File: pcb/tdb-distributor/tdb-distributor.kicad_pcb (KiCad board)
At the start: 2 copper layers, 81.3 x 63.5 mm, 15 parts, among them J1 Conn_02x07_Odd_Even, J2 Conn_02x07_Odd_Even, J3 Conn_02x07_Odd_Even, J4 Conn_02x07_Odd_Even, J5 Screw_Terminal_01x03, J6 Conn_01x06_Pin, J7 Conn_01x07_Pin, J8 Conn_01x08_Pin, U1 LM317_TO-220

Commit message: Add labels to power input
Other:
- board text added: "15V"
- board text added: "5V"
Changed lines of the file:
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@@
+    (effects (font (size 1 1) (thickness 0.15)) (justify left bottom))
+  )
+  (gr_text "15V" (at 138.43 41.91 -90) (layer "F.SilkS")
+    (effects (font (size 1 1) (thickness 0.15)) (justify left bottom))
+  )
+  (gr_text "5V" (at 138.43 36.83 -90) (layer "F.SilkS")
     (effects (font (size 1 1) (thickness 0.15)) (justify left bottom))
   )
@@
     (effects (font (size 1 1) (thickness 0.15)) (justify left bottom))
   )
+  (gr_text "GND\n" (at 138.43 46.99 -90) (layer "F.SilkS")
+    (effects (font (size 1 1) (thickness 0.15)) (justify left bottom))
+  )

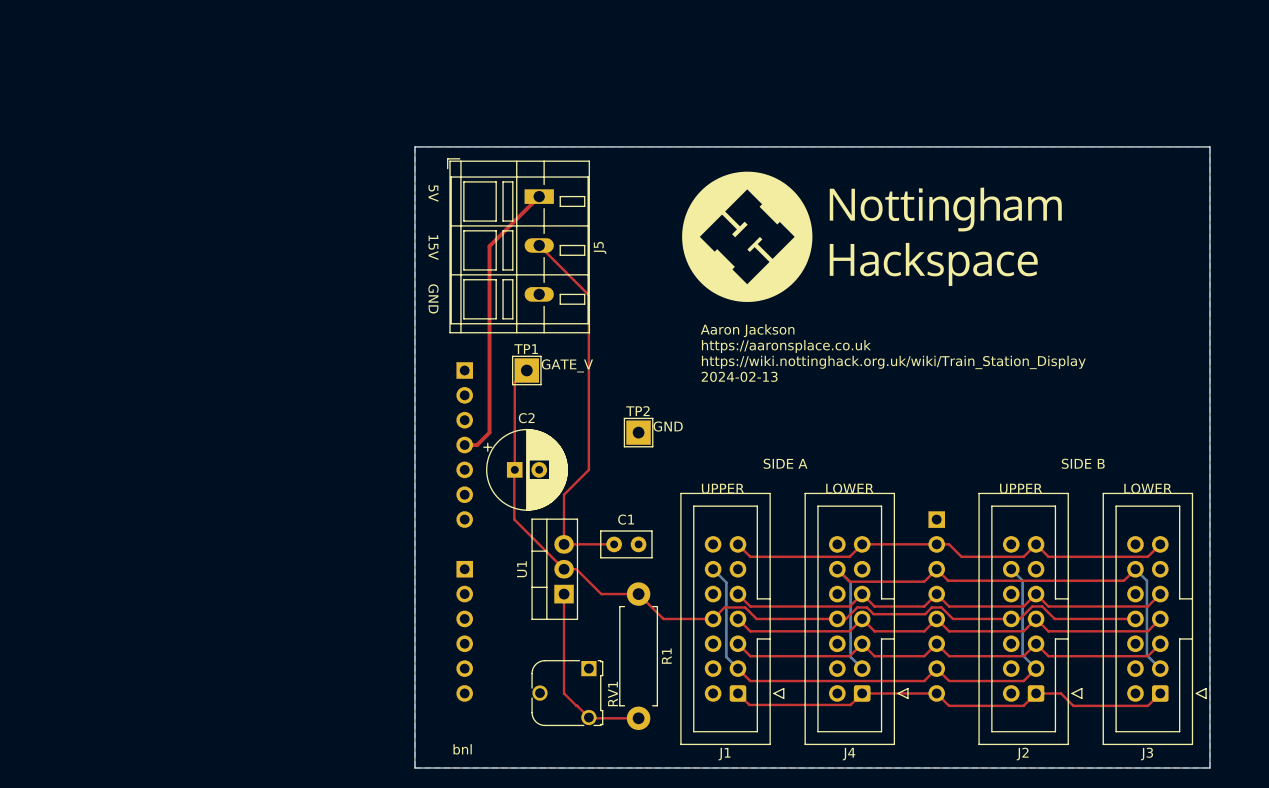
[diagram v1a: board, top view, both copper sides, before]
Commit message: Board redesign
Includes R7 MPU and WizNet
Adds buffer chips to hopefully support both sides of the display
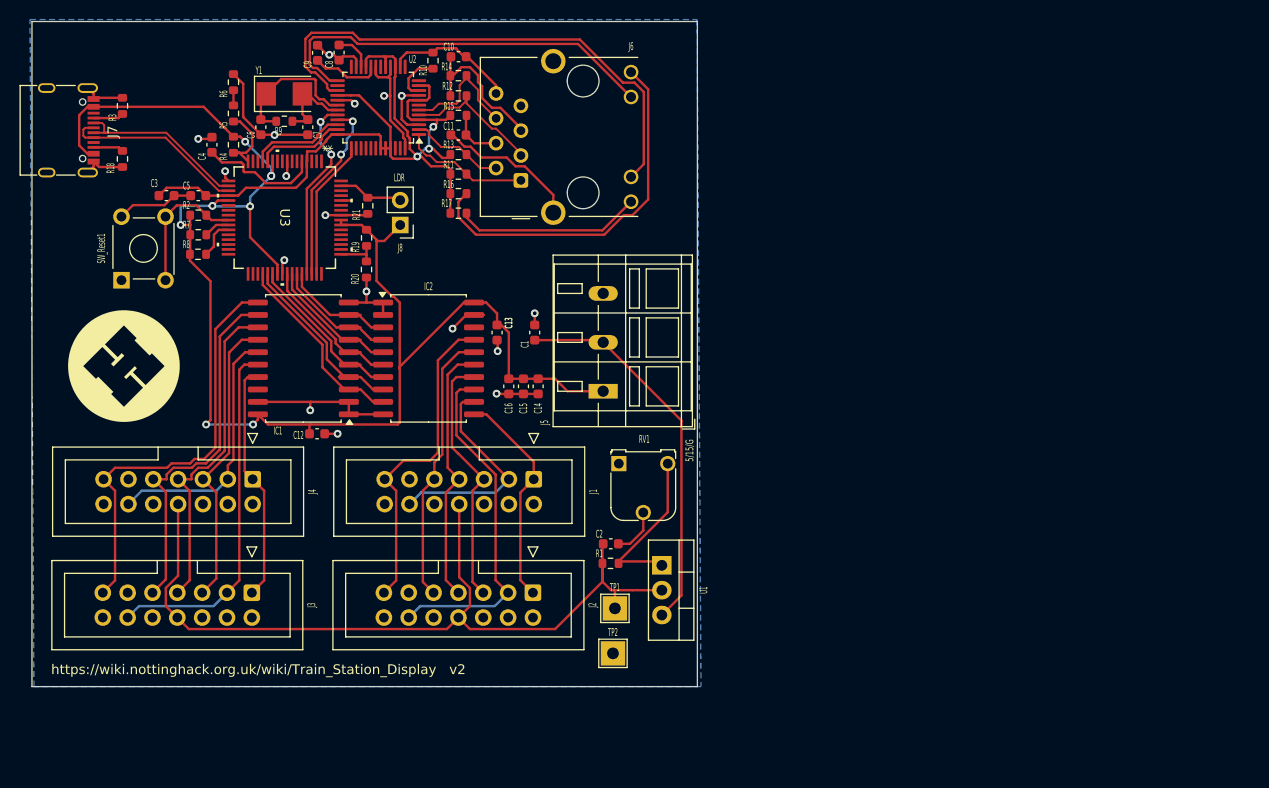
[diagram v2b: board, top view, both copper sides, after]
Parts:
- added C10: 10n, Capacitor_SMD:C_0603_1608Metric, F.Cu at (141.6, 23.8)
- added C11: 22n, Capacitor_SMD:C_0603_1608Metric, F.Cu at (141.6, 31.8)
- added C12: 4.7u, Capacitor_SMD:C_0603_1608Metric, F.Cu at (127.2, 62.4)
- added C13: 4.7u, Capacitor_SMD:C_0603_1608Metric, F.Cu at (145.6, 52.0)
- added C14: 22u, Capacitor_SMD:C_0603_1608Metric, F.Cu at (149.8, 57.5)
- added C15: 22u, Capacitor_SMD:C_0603_1608Metric, F.Cu at (148.2, 57.5)
- added C16: 22u, Capacitor_SMD:C_0603_1608Metric, F.Cu at (146.8, 57.5)
- added C3: 4.7u, Capacitor_SMD:C_0603_1608Metric, F.Cu at (111.8, 38.0)
- added C4: 4.7u, Capacitor_SMD:C_0603_1608Metric, F.Cu at (116.4, 32.8)
- added C5: 4.7u, Capacitor_SMD:C_0603_1608Metric, F.Cu at (115.0, 38.0)
- added C6: 18p, Capacitor_SMD:C_0603_1608Metric, F.Cu at (121.4, 31.0)
- added C7: 18p, Capacitor_SMD:C_0603_1608Metric, F.Cu at (126.2, 31.0)
- added C8: 10n, Capacitor_SMD:C_0603_1608Metric, F.Cu at (129.4, 23.4)
- added C9: 4.7u, Capacitor_SMD:C_0603_1608Metric, F.Cu at (127.2, 23.4)
- added IC1: 74HC541D,653, Package_SO:SOIC-20W_7.5x12.8mm_P1.27mm, F.Cu at (125.7, 54.6)
- added IC2: 74HC541D,653, Package_SO:SOIC-20W_7.5x12.8mm_P1.27mm, F.Cu at (138.5, 54.6)
- added R10: 12.4k, Resistor_SMD:R_0603_1608Metric, F.Cu at (139.0, 24.2)
- added R11: 49.9, Resistor_SMD:R_0603_1608Metric, F.Cu at (141.6, 35.8)
- added R12: 49.9, Resistor_SMD:R_0603_1608Metric, F.Cu at (141.6, 27.8)
- added R13: 49.9, Resistor_SMD:R_0603_1608Metric, F.Cu at (141.6, 33.8)
- added R14: 49.9, Resistor_SMD:R_0603_1608Metric, F.Cu at (141.6, 25.7)
- added R15: 10, Resistor_SMD:R_0603_1608Metric, F.Cu at (141.6, 29.8)
- added R16: 100, Resistor_SMD:R_0603_1608Metric, F.Cu at (141.6, 37.8)
- added R17: 100, Resistor_SMD:R_0603_1608Metric, F.Cu at (141.6, 39.8)
- added R18: 5.1k, Resistor_SMD:R_0603_1608Metric, F.Cu at (107.2, 34.2)
- added R19: 100k, Resistor_SMD:R_0603_1608Metric, F.Cu at (132.2, 42.3)
- added R2: 5.1k, Resistor_SMD:R_0603_1608Metric, F.Cu at (115.0, 40.0)
- added R20: 5.1k, Resistor_SMD:R_0603_1608Metric, F.Cu at (132.2, 45.5)
- added R21: 5.1k, Resistor_SMD:R_0603_1608Metric, F.Cu at (132.3, 39.0)
- added R3: 5.1k, Resistor_SMD:R_0603_1608Metric, F.Cu at (107.2, 28.8)
- added R4: 5.1k, Resistor_SMD:R_0603_1608Metric, F.Cu at (118.6, 32.8)
- added R5: 5.1k, Resistor_SMD:R_0603_1608Metric, F.Cu at (118.6, 29.6)
- added R6: 5.1k, Resistor_SMD:R_0603_1608Metric, F.Cu at (118.6, 26.4)
- added R7: 5.1k, Resistor_SMD:R_0603_1608Metric, F.Cu at (115.0, 42.0)
- added R8: 5.1k, Resistor_SMD:R_0603_1608Metric, F.Cu at (115.0, 44.0)
- added R9: 1M, Resistor_SMD:R_0603_1608Metric, F.Cu at (123.8, 30.4)
- added SW_Reset1: SW_Push, Button_Switch_THT:SW_TH_Tactile_Omron_B3F-10xx, F.Cu at (107.2, 46.6)
- added U2: W5500, Package_QFP:LQFP-48_7x7mm_P0.5mm, F.Cu at (133.4, 29.0)
- added U3: R7FA4M1AB3CFM, R7FA4M1AB3CFM:PLQP0064KB-C_REN, F.Cu at (123.8, 40.3)
- added Y1: 25M, Crystal:Crystal_SMD_5032-2Pin_5.0x3.2mm, F.Cu at (123.8, 27.6)
- C1: footprint Capacitor_THT:C_Disc_D5.0mm_W2.5mm_P2.50mm -> Capacitor_SMD:C_0603_1608Metric
- C2: footprint Capacitor_THT:CP_Radial_D8.0mm_P2.50mm -> Capacitor_SMD:C_0603_1608Metric
- J6: value Conn_01x06_Pin -> RJ45_Hanrun_HR911105A_Horizontal; footprint Connector_PinHeader_2.54mm:PinHeader_1x06_P2.54mm_Vertical -> Connector_RJ:RJ45_Hanrun_HR911105A_Horizontal; moved to F.Cu
- J7: value Conn_01x07_Pin -> USB_C_Receptacle_USB2.0_16P; footprint Connector_PinHeader_2.54mm:PinHeader_1x07_P2.54mm_Vertical -> Connector_USB:USB_C_Receptacle_G-Switch_GT-USB-7010ASV; moved to F.Cu
- J8: value Conn_01x08_Pin -> Conn_01x02; footprint Connector_PinHeader_2.54mm:PinHeader_1x08_P2.54mm_Vertical -> Connector_PinHeader_2.54mm:PinHeader_1x02_P2.54mm_Vertical; moved to F.Cu
- R1: footprint Resistor_THT:R_Axial_DIN0411_L9.9mm_D3.6mm_P12.70mm_Horizontal -> Resistor_SMD:R_0603_1608Metric
- moved J3 93.4 mm to (120.5, 78.6), turned to -90 degrees
- moved J4 66.1 mm to (120.6, 67.0), turned to -90 degrees
- moved J8 62.6 mm to (135.7, 41.0)
- moved J2 52.5 mm to (149.2, 78.6), turned to -90 degrees
- moved J7 48.4 mm to (100.6, 31.3), turned to -90 degrees
- moved J6 40.2 mm to (148.0, 36.4), turned to 90 degrees
- moved J1 30.3 mm to (149.3, 67.0), turned to -90 degrees
- moved TP1 25.9 mm to (157.6, 80.2)
- moved C1 23.1 mm to (149.4, 52.0), turned to 90 degrees
- moved TP2 22.7 mm to (157.4, 84.8)
- moved RV1 21.2 mm to (158.0, 65.4), turned to 0 degrees
- moved J5 20.9 mm to (156.4, 58.0), turned to 90 degrees
- moved C2 12.4 mm to (157.2, 73.6)
- moved U1 10.4 mm to (162.4, 75.8), turned to -90 degrees
- moved R1 4.25 mm to (157.2, 75.6), turned to 0 degrees
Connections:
- J1 pad 1: /CLOCK -> /bCLOCK
- J1 pad 11: GND -> unconnected-(J1-Pin_11-Pad11)
- J1 pad 12: /DATA_A -> /bDATA_A
- J1 pad 13: /STROBE -> /bSTROBE
- J1 pad 3: /DATA_A -> /bDATA_A
- J1 pad 5: /BCD_A -> /bBCD_A
- J1 pad 7: /BCD_B -> /bBCD_B
- J1 pad 9: /BCD_C -> /bBCD_C
- J2 pad 1: /CLOCK -> /bCLOCK
- J2 pad 11: GND -> unconnected-(J2-Pin_11-Pad11)
- J2 pad 12: /DATA_A -> /bDATA_B
- J2 pad 13: /STROBE -> /bSTROBE
- J2 pad 3: /DATA_A -> /bDATA_B
- J2 pad 5: /BCD_A -> /bBCD_A
- J2 pad 7: /BCD_B -> /bBCD_B
- J2 pad 9: /BCD_C -> /bBCD_C
- J3 pad 1: /CLOCK -> /aCLOCK
- J3 pad 11: GND -> unconnected-(J3-Pin_11-Pad11)
- J3 pad 12: /DATA_B -> /aDATA_A
- J3 pad 13: /STROBE -> /aSTROBE
- J3 pad 3: /DATA_B -> /aDATA_A
- J3 pad 5: /BCD_A -> /aBCD_A
- J3 pad 7: /BCD_B -> /aBCD_B
- J3 pad 9: /BCD_C -> /aBCD_C
- J4 pad 1: /CLOCK -> /aCLOCK
- J4 pad 11: GND -> unconnected-(J4-Pin_11-Pad11)
- J4 pad 12: /DATA_B -> /aDATA_B
- J4 pad 13: /STROBE -> /aSTROBE
- J4 pad 3: /DATA_B -> /aDATA_B
- J4 pad 5: /BCD_A -> /aBCD_A
- J4 pad 7: /BCD_B -> /aBCD_B
- J4 pad 9: /BCD_C -> /aBCD_C
- J6 pad 1: unconnected-(J6-Pin_1-Pad1) -> TXOP
- J6 pad 2: unconnected-(J6-Pin_2-Pad2) -> TXON
- J6 pad 3: unconnected-(J6-Pin_3-Pad3) -> RXIP
- J6 pad 4: unconnected-(J6-Pin_4-Pad4) -> Net-(J6-TCT)
- J6 pad 5: unconnected-(J6-Pin_5-Pad5) -> Net-(J6-RCT)
- J6 pad 6: unconnected-(J6-Pin_6-Pad6) -> RXIN
- J8 pad 1: unconnected-(J8-Pin_1-Pad1) -> +5V
- J8 pad 2: /STROBE -> Net-(J8-Pin_2)
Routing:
- net GND: track 0.00 -> 132.2 mm, vias 0 -> 17
- net +5V: track 29.3 -> 157.0 mm, vias 0 -> 8
- net +3.3V: track 0.00 -> 85.4 mm, vias 0 -> 3
- net /DATA_A: track 55.0 -> 0.00 mm
- net /DATA_B: track 54.9 -> 0.00 mm
- net ACTLED: track 0.00 -> 53.9 mm
- net /BCD_C: track 47.4 -> 0.00 mm
- net /BCD_A: track 47.4 -> 0.00 mm
- net /BCD_B: track 47.4 -> 0.00 mm
- net /STROBE: track 46.3 -> 0.00 mm
- net /CLOCK: track 46.3 -> 0.00 mm
- net /aSTROBE: track 0.00 -> 43.0 mm
- net LINKLED: track 0.00 -> 41.5 mm
- net /aBCD_C: track 0.00 -> 38.4 mm
- net Net-(J6-Pad12): track 0.00 -> 38.1 mm
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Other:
- board size 81.3 x 63.5 mm -> 68 x 68 mm
- board text added: "5/15/G"
- board text added: "LDR"
- board text added: "https://wiki.nottinghack.org.uk/wiki/Train_Station_Display v2"
- board text removed: "15V"
- board text removed: "5V"
- board text removed: "Aaron Jackson https://aaronsplace.co.uk https://wiki.nottinghack.org.uk/wiki/Train_Station_Display 2024-02-13"
- board text removed: "GATE_V"
- board text removed: "GND"
- board text removed: "LOWER"
- board text removed: "SIDE A"
- board text removed: "SIDE B"
- board text removed: "UPPER"
- board text removed: "bnl"

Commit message: minor drc cleanup
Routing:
- net unconnected-(U3-P004-Pad60): track 0.96 -> 0.00 mm
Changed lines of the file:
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@@
-	)
-	(segment
-		(start 129.6 38.499874)
-		(end 130.559874 38.499874)
-		(width 0.25)
-		(layer "F.Cu")
-		(net 99)
 	)
 	(segment
